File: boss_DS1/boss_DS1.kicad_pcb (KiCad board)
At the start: 2 copper layers, 80 x 100 mm, 86 parts, among them J2 Jack_6.35, J3 Conn_01x05, J4 Conn_01x05, J5 Conn_01x05, J6 Jack_6.35, J7 Conn_01x01_Socket, J8 Conn_01x01_Socket, J9 Barrel_Jack_Switch, P1 boss_DS1_front_panel, Q1 MMBT5551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

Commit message: Updated front.
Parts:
- added P2: bottom_panel, pedale:bottom_plate, F.Cu at (50.0, 50.0)
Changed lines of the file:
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@@
 		)
 		(embedded_fonts no)
-		(model "${KICAD9_3DMODEL_DIR}/Battery.3dshapes/BatteryHolder_Eagle_12BH611-GR.wrl"
+		(model "${KIPRJMOD}/../pedale.pretty/9V-battery_holder.step"
 			(offset
-				(xyz 0 0 0)
+				(xyz -25 6.5 0)
 			)
 			(scale
@@
 			)
 			(rotate
-				(xyz 0 0 0)
+				(xyz -0 -0 -0)
 			)
 		)
@@
 		(model "${KIPRJMOD}/../pedale.pretty/M3x8 Philips Screw.stp"
 			(offset
-				(xyz 0 0 -1.5)
+				(xyz 0 0 -8)
 			)
 			(scale
@@
 			)
 		)
+		(model "${KIPRJMOD}/../pedale.pretty/Abstandhalter M3 IG-AG 5mm+6mm - PA 66.stp"
+			(offset
+				(xyz 0 0 -4)
+			)
+			(scale
+				(xyz 1 1 1)
+			)
+			(rotate
+				(xyz -0 90 -0)
+			)
+		)
 	)
 	(footprint "Resistor_SMD:R_0603_1608Metric_Pad0.98x0.95mm_HandSolder"
@@
 		(model "${KIPRJMOD}/../pedale.pretty/M3x8 Philips Screw.stp"
 			(offset
-				(xyz 0 0 -1.5)
+				(xyz 0 0 -8)
 			)
 			(scale
@@
 			)
 		)
+		(model "${KIPRJMOD}/../pedale.pretty/Abstandhalter M3 IG-AG 5mm+6mm - PA 66.stp"
+			(offset
+				(xyz 0 0 -4)
+			)
+			(scale
+				(xyz 1 1 1)
+			)
+			(rotate
+				(xyz -0 90 -0)
+			)
+		)
 	)
 	(footprint "Resistor_SMD:R_0603_1608Metric_Pad0.98x0.95mm_HandSolder"
@@
 		)
 	)
+	(footprint "pedale:bottom_plate"
+		(layer "F.Cu")
+		(at 50 50)
+		(property "Reference" "P2"
+			(at 0 -0.5 0)
+			(unlocked yes)
+			(layer "F.SilkS")
+			(hide yes)
+			(effects
+				(font
+					(size 1 1)
+					(thickness 0.1)
+				)
+			)
+		)
+		(property "Value" "bottom_panel"
+			(at 0 1 0)
+			(unlocked yes)
+			(layer "F.Fab")
+			(effects
+				(font
+					(size 1 1)
+					(thickness 0.15)
+				)
+			)
+		)
+		(property "Datasheet" ""
+			(at 0 0 0)
+			(unlocked yes)
+			(layer "F.Fab")
+			(hide yes)
+			(effects
+				(font
+					(size 1 1)
+					(thickness 0.15)
+				)
+			)
+		)
+		(property "Description" "Potentiometer"
+			(at 0 0 0)
+			(unlocked yes)
+			(layer "F.Fab")
+			(hide yes)
+			(effects
+				(font
+					(size 1 1)
+					(thickness 0.15)
+				)
+			)
+		)
+		(property ki_fp_filters "Potentiometer*")
+		(sheetname "/")
+		(sheetfile "boss_DS1.kicad_sch")
+		(attr through_hole exclude_from_bom dnp)
+		(fp_rect
+			(start -0.1 -0.1)
+			(end 0.1 0.1)
+			(stroke
+				(width 0.05)
+				(type default)
+			)
+			(fill no)
+			(layer "B.CrtYd")
+		)
+		(fp_text user "${REFERENCE}"
+			(at 0 2.5 0)
+			(unlocked yes)
+			(layer "F.Fab")
+			(effects
+				(font
+					(size 1 1)
+					(thickness 0.15)
+				)
+			)
+		)
+		(embedded_fonts no)
+		(model "${KIPRJMOD}/../bottom_plate.step"
+			(offset
+				(xyz 0 0 -8)
+			)
+			(scale
+				(xyz 1 1 1)
+			)
+			(rotate
+				(xyz -0 -0 -0)
+			)
+		)
+	)
 	(footprint "Resistor_SMD:R_0603_1608Metric_Pad0.98x0.95mm_HandSolder"
 		(layer "F.Cu")
@@
 		(model "${KIPRJMOD}/../pedale.pretty/M3x8 Philips Screw.stp"
 			(offset
-				(xyz 0 0 -1.5)
+				(xyz 0 0 -8)
 			)
 			(scale
@@
 			)
 		)
+		(model "${KIPRJMOD}/../pedale.pretty/Abstandhalter M3 IG-AG 5mm+6mm - PA 66.stp"
+			(offset
+				(xyz 0 0 -4)
+			)
+			(scale
+				(xyz 1 1 1)
+			)
+			(rotate
+				(xyz -0 90 -0)
+			)
+		)
 	)
 	(footprint "Capacitor_SMD:C_0603_1608Metric_Pad1.08x0.95mm_HandSolder"
@@
 		(model "${KIPRJMOD}/../pedale.pretty/M3x8 Philips Screw.stp"
 			(offset
-				(xyz 0 0 -1.5)
+				(xyz 0 0 -8)
 			)
 			(scale
@@
 			)
 		)
+		(model "${KIPRJMOD}/../pedale.pretty/Abstandhalter M3 IG-AG 5mm+6mm - PA 66.stp"
+			(offset
+				(xyz 0 0 -4)
+			)
+			(scale
+				(xyz 1 1 1)
+			)
+			(rotate
+				(xyz -0 90 -0)
+			)
+		)
 	)
 	(footprint "Resistor_SMD:R_0603_1608Metric_Pad0.98x0.95mm_HandSolder"
@@
 		(model "${KIPRJMOD}/../pedale.pretty/M3x8 Philips Screw.stp"
 			(offset
-				(xyz 0 0 -1.5)
+				(xyz 0 0 -8)
 			)
 			(scale
@@
 			)
 		)
+		(model "${KIPRJMOD}/../pedale.pretty/Abstandhalter M3 IG-AG 5mm+6mm - PA 66.stp"
+			(offset
+				(xyz 0 0 -4)
+			)
+			(scale
+				(xyz 1 1 1)
+			)
+			(rotate
+				(xyz -0 90 -0)
+			)
+		)

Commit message: Updated libs.
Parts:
- SW1: footprint pedale:foot_switch_tht_and_floating -> pedale:foot_switch_tht_no_pad
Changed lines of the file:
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@@
 		(sheetfile "boss_DS1.kicad_sch")
 		(attr through_hole exclude_from_bom dnp)
-		(fp_line
-			(start 26.4 18.23)
-			(end 26.4 -2)
-			(stroke
-				(width 0.05)
-				(type solid)
-			)
-			(layer "F.CrtYd")
-		)
-		(fp_line
-			(start 26.4 -2)
-			(end -7.45 -2)
-			(stroke
-				(width 0.05)
-				(type solid)
-			)
-			(layer "F.CrtYd")
-		)
-		(fp_line
-			(start -7.45 18.23)
-			(end 26.4 18.23)
-			(stroke
-				(width 0.05)
-				(type solid)
-			)
-			(layer "F.CrtYd")
-		)
-		(fp_line
-			(start -7.45 18.23)
-			(end -7.45 -2)
+		(fp_rect
+			(start -7 -1)
+			(end 26.4 17.3)
 			(stroke
 				(width 0.05)
-				(type solid)
+				(type default)
 			)
+			(fill no)
 			(layer "F.CrtYd")
 		)
@@
 		(sheetfile "boss_DS1.kicad_sch")
 		(attr through_hole exclude_from_bom dnp)
-		(fp_line
-			(start 3.1 8.75)
-			(end -51.4 8.75)
-			(stroke
-				(width 0.12)
-				(type solid)
-			)
-			(layer "F.SilkS")
-		)
-		(fp_line
-			(start 3.1 -21.45)
-			(end 3.1 8.75)
-			(stroke
-				(width 0.12)
-				(type solid)
-			)
-			(layer "F.SilkS")
-		)
-		(fp_line
-			(start -51.4 8.75)
-			(end -51.4 -21.45)
-			(stroke
-				(width 0.12)
-				(type solid)
-			)
-			(layer "F.SilkS")
-		)
-		(fp_line
-			(start -51.4 -21.45)
-			(end 3.1 -21.45)
-			(stroke
-				(width 0.12)
-				(type solid)
-			)
-			(layer "F.SilkS")
-		)
-		(fp_line
-			(start 3.6 9.25)
-			(end -51.9 9.25)
-			(stroke
-				(width 0.05)
-				(type solid)
-			)
-			(layer "F.CrtYd")
-		)
-		(fp_line
-			(start 3.6 -21.95)
-			(end 3.6 9.25)
-			(stroke
-				(width 0.05)
-				(type solid)
-			)
-			(layer "F.CrtYd")
-		)
-		(fp_line
-			(start -51.9 9.25)
-			(end -51.9 -21.95)
-			(stroke
-				(width 0.05)
-				(type solid)
-			)
-			(layer "F.CrtYd")
-		)
-		(fp_line
-			(start -51.9 -21.95)
-			(end 3.6 -21.95)
+		(fp_rect
+			(start -51.4 -21.4)
+			(end 3.1 8.8)
 			(stroke
 				(width 0.05)
-				(type solid)
+				(type default)
 			)
+			(fill no)
 			(layer "F.CrtYd")
 		)
@@
 		)
 	)
-	(footprint "pedale:foot_switch_tht_and_floating"
+	(footprint "pedale:foot_switch_tht_no_pad"
 		(locked yes)
 		(layer "F.Cu")
@@
 		(attr through_hole exclude_from_bom dnp)
 		(fp_rect
-			(start -14.2 -13.2)
-			(end 14.2 13.2)
+			(start -9.2 -7.7)
+			(end 9.2 7.7)
 			(stroke
 				(width 0.05)
@@
 			(layer "F.CrtYd")
 		)
+		(fp_rect
+			(start -9 -7.5)
+			(end 9 7.5)
+			(stroke
+				(width 0.15)
+				(type default)
+			)
+			(fill no)
+			(layer "F.Fab")
+		)
 		(fp_text user "${REFERENCE}"
 			(at -0.1 -10.875 0)
@@
 		)
 		(pad "1" thru_hole roundrect
-			(at -7.1 -5 180)
-			(size 8.8 11.6)
-			(drill oval 2 4
-				(offset 2.4 2.2)
-			)
+			(at -7.1 -4.5 180)
+			(size 4 5)
+			(drill oval 2 3)
 			(layers "*.Cu" "*.Mask")
 			(remove_unused_layers no)
-			(roundrect_rratio 0.1136363636)
+			(roundrect_rratio 0.25)
 			(net 22 "/SW_ON")
 			(pinfunction "A")
@@
 		)
 		(pad "2" thru_hole roundrect
-			(at 0 -5)
-			(size 4 11.5)
-			(drill oval 2 4
-				(offset 0 -2.25)
-			)
+			(at 0 -4.5)
+			(size 4 5)
+			(drill oval 2 3)
 			(layers "*.Cu" "*.Mask")
 			(remove_unused_layers no)
@@
 		)
 		(pad "3" thru_hole roundrect
-			(at 7.1 -5 180)
-			(size 8.9 11.5)
-			(drill oval 2 4
-				(offset -2.45 2.25)
-			)
+			(at 7.1 -4.5 180)
+			(size 4 5)
+			(drill oval 2 3)
 			(layers "*.Cu" "*.Mask")
 			(remove_unused_layers no)
-			(roundrect_rratio 0.1123595506)
+			(roundrect_rratio 0.25)
 			(net 31 "Net-(SW1A-C)")
 			(pinfunction "C")
@@
 		)
 		(pad "4" thru_hole roundrect
-			(at 7.1 5)
-			(size 8.9 11.5)
-			(drill oval 2 4
-				(offset 2.45 2.25)
-			)
+			(at 7.1 4.5)
+			(size 4 5)
+			(drill oval 2 3)
 			(layers "*.Cu" "*.Mask")
 			(remove_unused_layers no)
-			(roundrect_rratio 0.1123595506)
+			(roundrect_rratio 0.25)
 			(net 11 "9V")
 			(pinfunction "A")
@@
 		)
 		(pad "5" thru_hole roundrect
-			(at 0 5)
-			(size 4 11.5)
-			(drill oval 2 4
-				(offset 0 2.25)
-			)
+			(at 0 4.5)
+			(size 4 5)
+			(drill oval 2 3)
 			(layers "*.Cu" "*.Mask")
 			(remove_unused_layers no)
@@
 		)
 		(pad "6" thru_hole roundrect
-			(at -7.1 5)
-			(size 8.9 11.5)
-			(drill oval 2 4
-				(offset -2.45 2.25)
-			)
+			(at -7.1 4.5)
+			(size 4 5)
+			(drill oval 2 3)
 			(layers "*.Cu" "*.Mask")
 			(remove_unused_layers no)
-			(roundrect_rratio 0.1123595506)
+			(roundrect_rratio 0.25)
 			(net 28 "unconnected-(SW1B-C-Pad6)")
 			(pinfunction "C")
@@
 		(sheetfile "boss_DS1.kicad_sch")
 		(attr through_hole exclude_from_bom dnp)
-		(fp_line
-			(start -7.45 18.23)
-			(end -7.45 -2)
-			(stroke
-				(width 0.05)
-				(type solid)
-			)
-			(layer "F.CrtYd")
-		)
-		(fp_line
-			(start -7.45 18.23)
-			(end 26.4 18.23)
-			(stroke
-				(width 0.05)
-				(type solid)
-			)
-			(layer "F.CrtYd")
-		)
-		(fp_line
-			(start 26.4 -2)
-			(end -7.45 -2)
-			(stroke
-				(width 0.05)
-				(type solid)
-			)
-			(layer "F.CrtYd")
-		)
-		(fp_line
-			(start 26.4 18.23)
-			(end 26.4 -2)
+		(fp_rect
+			(start -7 -1)
+			(end 26.4 17.3)
 			(stroke
 				(width 0.05)
-				(type solid)
+				(type default)
 			)
+			(fill no)
 			(layer "F.CrtYd")
 		)

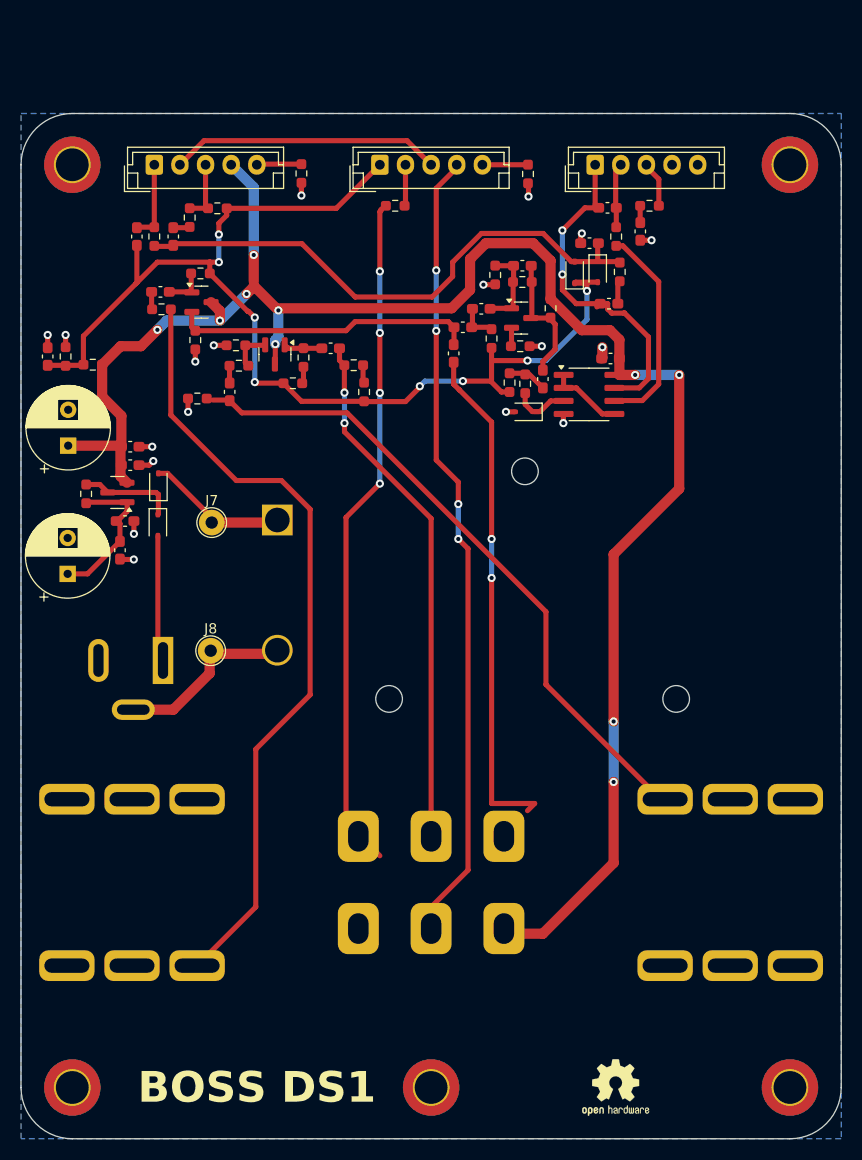
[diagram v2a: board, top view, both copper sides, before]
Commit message: Potentiometers checked.
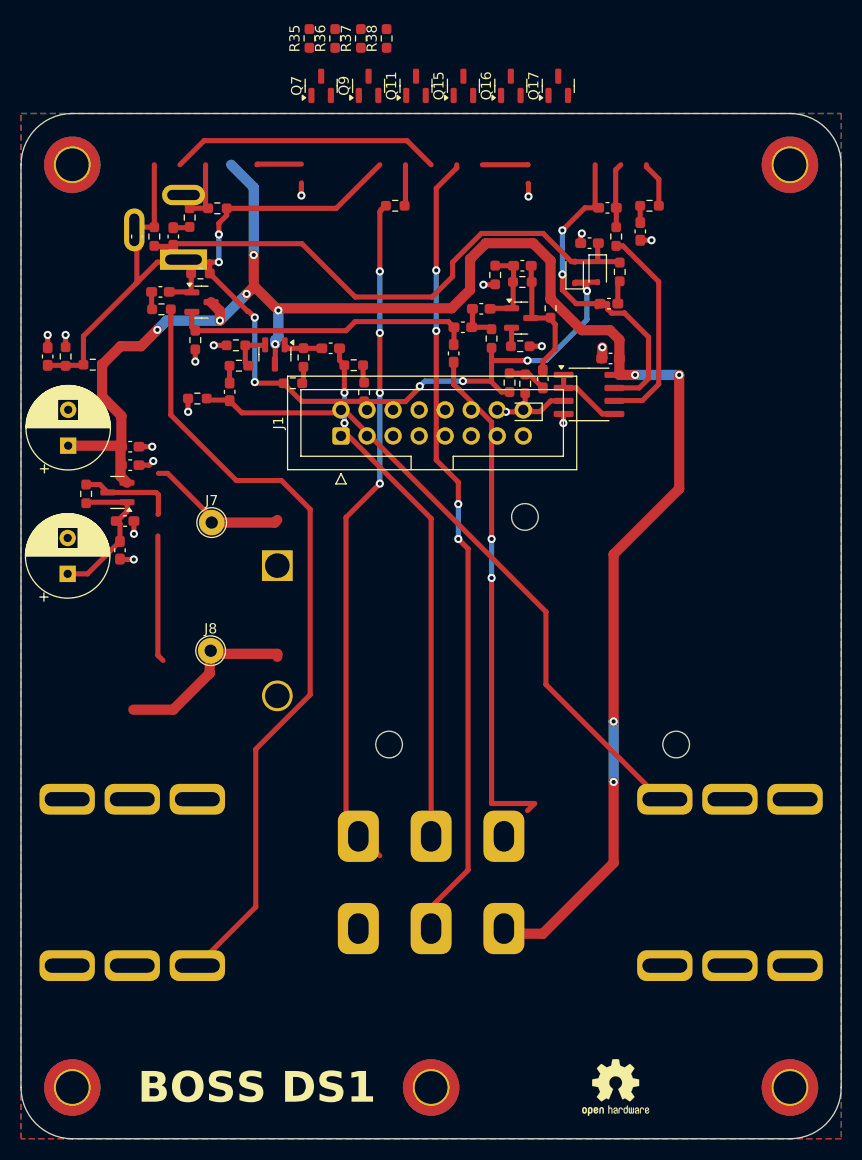
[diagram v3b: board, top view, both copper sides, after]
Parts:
- removed D3, D5: 1N4148WS, Diode_SMD:D_SOD-323
- removed J3, J4, J5: Conn_01x05, Connector_JST:JST_EH_B5B-EH-A_1x05_P2.50mm_Vertical
- removed R18, R8: 1k, Resistor_SMD:R_0603_1608Metric_Pad0.98x0.95mm_HandSolder
- removed RV1, RV7, RV9: floating_pot_knob, pedale:floating_pot_knob
- removed RV5, RV6, RV8: floating_pot, pedale:floating_pot
- added J1: top_panel_connector, Connector_IDC:IDC-Header_2x08_P2.54mm_Vertical, F.Cu at (81.2, 81.5)
- added Q11: AO3401A, Package_TO_SOT_SMD:SOT-23, F.Cu at (88.5, 47.3)
- added Q15: AO3400A, Package_TO_SOT_SMD:SOT-23, F.Cu at (93.2, 47.3)
- added Q16: AO3400A, Package_TO_SOT_SMD:SOT-23, F.Cu at (97.8, 47.3)
- added Q17: AO3400A, Package_TO_SOT_SMD:SOT-23, F.Cu at (102.4, 47.3)
- added Q7: AO3401A, Package_TO_SOT_SMD:SOT-23, F.Cu at (79.3, 47.3)
- added Q9: AO3401A, Package_TO_SOT_SMD:SOT-23, F.Cu at (83.9, 47.3)
- added R35: 100k, Resistor_SMD:R_0603_1608Metric_Pad0.98x0.95mm_HandSolder, F.Cu at (78.1, 42.7)
- added R36: 100k, Resistor_SMD:R_0603_1608Metric_Pad0.98x0.95mm_HandSolder, F.Cu at (80.6, 42.7)
- added R37: 2.2k, Resistor_SMD:R_0603_1608Metric_Pad0.98x0.95mm_HandSolder, F.Cu at (83.2, 42.7)
- added R38: 2.2k, Resistor_SMD:R_0603_1608Metric_Pad0.98x0.95mm_HandSolder, F.Cu at (85.7, 42.7)
- moved J2 48.4 mm to (67.2, 133.1), turned to 180 degrees
- moved J6 48.4 mm to (112.8, 116.9), turned to 0 degrees
- moved J9 39.2 mm to (65.8, 64.2), turned to 180 degrees
- moved BT1 4.45 mm to (75.0, 94.1)
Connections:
- net Net-(BT1-+) renamed BAT+
- net Net-(BT1--) renamed BAT-
- net Net-(C11-Pad2) renamed /OUTPUT
- net Net-(D3-K) renamed REG_IN
- net Net-(J6-PadT) renamed /INPUT
- J2 pad R: 0 -> unconnected-(J2-PadR)
- J6 pad R: 0 -> unconnected-(J6-PadR)
- J6 pad SN: unconnected-(J6-PadSN) -> IN_CONNECT
- J9 pad 1: Net-(D3-A) -> CONN+
- J9 pad 2: 0 -> CONN-
- SW1 pad 4: 9V -> unconnected-(SW1B-A-Pad4)
- SW1 pad 6: unconnected-(SW1B-C-Pad6) -> 9V
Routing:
- net TONE_OUT: track 26.4 -> 0.00 mm
- net Net-(J1A-Pin_6): track 33.6 -> 60.0 mm
- net Net-(D3-A): track 12.4 -> 0.00 mm
- net CONN+: track 0.00 -> 12.4 mm
- net (no net): track 0.00 -> 8.83 mm
- net Net-(J5-Pin_5): track 4.46 -> 0.00 mm
- net Net-(J4-Pin_5): track 4.38 -> 0.00 mm
- added copper zone on F.Cu, net 0

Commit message: Rutiranje gotovo
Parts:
- removed SIM1: Logo_Open_Hardware_Small, Symbol:OSHW-Logo2_7.3x6mm_SilkScreen
- moved R38 82.7 mm to (78.0, 125.0)
- moved Q17 56.7 mm to (54.3, 77.3)
- moved C14 50.3 mm to (102.8, 72.7)
- moved R23 50.3 mm to (104.6, 72.7)
- moved R13 50.0 mm to (112.1, 81.5), turned to -90 degrees
- moved R22 49.3 mm to (106.3, 74.6), turned to 90 degrees
- moved C9 48.8 mm to (110.3, 81.5), turned to 90 degrees
- moved Q16 48.4 mm to (52.5, 64.3), turned to 180 degrees
- moved R17 47.7 mm to (114.2, 79.3)
- moved Q15 45.5 mm to (52.5, 67.7), turned to 0 degrees
- moved Q1 44.6 mm to (111.3, 77.5), turned to 90 degrees
- moved R35 43.9 mm to (55.0, 80.0), turned to 180 degrees
- moved R15 42.8 mm to (108.6, 77.5), turned to 90 degrees
- moved R37 42.3 mm to (106.3, 78.1), turned to -90 degrees
- moved R36 40.8 mm to (55.3, 74.6), turned to 180 degrees
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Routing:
- net IN_CONNECT: track 0.00 -> 118.3 mm, vias 0 -> 2
- net Net-(SW1B-B): track 76.0 -> 13.5 mm, vias 4 -> 0
- net Net-(J1D-Pin_8): track 0.00 -> 54.7 mm, vias 0 -> 1
- net 4V5: track 110.4 -> 56.1 mm, vias 8 -> 4
- net BAT-: track 18.0 -> 68.4 mm
- net /INPUT: track 76.8 -> 35.9 mm
- net OP_OUT: track 54.0 -> 15.5 mm, vias 0 -> 2
- net Net-(J1A-Pin_6): track 60.0 -> 27.2 mm
- net BAT+: track 13.5 -> 38.3 mm
- net CONN-: track 0.00 -> 24.8 mm
- net Net-(J1E-Pin_10): track 0.00 -> 23.9 mm, vias 0 -> 2
- net IN_BUFF: track 29.5 -> 6.02 mm
- net Net-(U1B--): track 20.6 -> 2.17 mm
- net Net-(D4-K): track 5.57 -> 23.6 mm
- net REG_IN: track 9.39 -> 26.9 mm
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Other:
- board text removed: "BOSS DS1"

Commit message: Updated all.
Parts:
- J1: footprint Connector_IDC:IDC-Header_2x08_P2.54mm_Vertical -> pedale:IDC-Header_2x08_P2.54mm_Vertical
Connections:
- C20 pad 1: Net-(J1A-Pin_6) -> Net-(J1C-Pin_16)
- C20 pad 2: Net-(J1A-Pin_4) -> Net-(J1C-Pin_14)
- C26 pad 1: Net-(J1B-Pin_5) -> Net-(J1A-Pin_6)
- C7 pad 1: Net-(J1A-Pin_6) -> Net-(J1C-Pin_16)
- J1 pad 12: TONE_OUT -> Net-(J1C-Pin_12)
- J1 pad 16: 4V5 -> Net-(J1C-Pin_16)
- J1 pad 4: Net-(J1A-Pin_4) -> TONE_OUT
- J1 pad 5: Net-(J1B-Pin_5) -> TONE_OUT
- J1 pad 7: TONE_OUT -> Net-(J1B-Pin_7)
- J1 pad 9: Net-(J1B-Pin_9) -> 4V5
- R28 pad 2: Net-(J1B-Pin_9) -> Net-(J1A-Pin_2)
- R29 pad 1: Net-(J1B-Pin_9) -> Net-(J1A-Pin_2)
- R30 pad 2: Net-(J1B-Pin_5) -> Net-(J1A-Pin_6)
- R31 pad 1: Net-(J1C-Pin_14) -> Net-(J1B-Pin_7)
- R4 pad 2: Net-(J1A-Pin_2) -> Net-(J1C-Pin_12)
- R6 pad 2: Net-(J1A-Pin_4) -> Net-(J1C-Pin_14)
- U1 pad 7: Net-(J1A-Pin_6) -> Net-(J1C-Pin_16)
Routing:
- net Net-(J1C-Pin_16): track 0.00 -> 37.3 mm, vias 0 -> 4
- net Net-(J1B-Pin_5): track 19.7 -> 0.00 mm, vias 2 -> 0
- net Net-(J1B-Pin_7): track 0.00 -> 18.0 mm
- net Net-(J1A-Pin_4): track 16.8 -> 0.00 mm, vias 2 -> 0
- net Net-(J1A-Pin_2): track 4.82 -> 20.9 mm
- net Net-(J1C-Pin_12): track 0.00 -> 15.4 mm, vias 0 -> 1
- net Net-(J1C-Pin_14): track 10.4 -> 24.7 mm, vias 0 -> 4
- net Net-(J1B-Pin_9): track 14.1 -> 0.00 mm
- net 4V5: track 56.1 -> 68.1 mm, vias 4 -> 5
- net Net-(J1A-Pin_6): track 27.2 -> 18.6 mm
- net TONE_OUT: track 6.13 -> 3.59 mm
- net Net-(J1E-Pin_10): vias 2 -> 3
